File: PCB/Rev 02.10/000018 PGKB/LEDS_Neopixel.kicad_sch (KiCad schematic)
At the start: 15 parts

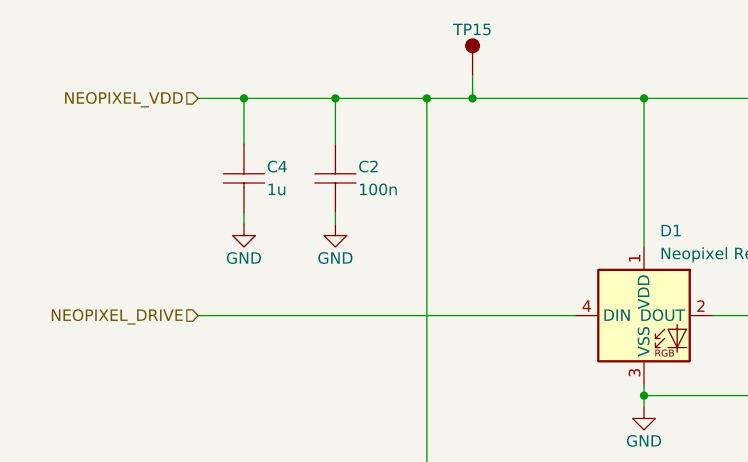
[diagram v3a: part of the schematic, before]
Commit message: Resolved DRC problems
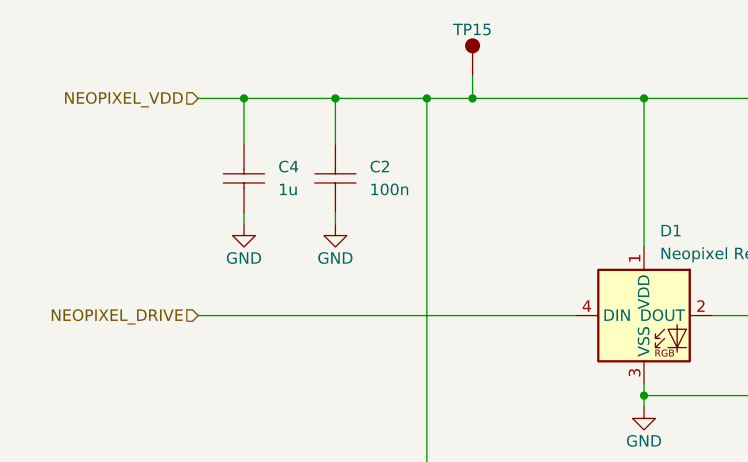
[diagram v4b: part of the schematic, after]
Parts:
- C4: Code 1u -> (none)
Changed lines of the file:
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@@
 			)
 		)
-		(property "Description" ""
+		(property "Description" "Power symbol creates a global label with name \"GND\" , ground"
 			(at 127 172.72 0)
 			(effects
@@
 		(on_board yes)
 		(dnp no)
+		(fields_autoplaced yes)
 		(property "Reference" "C2"
-			(at 95.25 31.75 0)
+			(at 96.52 31.7499 0)
 			(effects
 				(font
@@
 		)
 		(property "Value" "100n"
-			(at 95.25 34.29 0)
+			(at 96.52 34.2899 0)
 			(effects
 				(font
@@
 			)
 		)
-		(property "Description" ""
+		(property "Description" "CAP CER 0.1UF 50V X7R 0603"
 			(at 92.71 33.02 0)
 			(effects
@@
 			)
 		)
-		(property "Description" ""
+		(property "Description" "Power symbol creates a global label with name \"GND\" , ground"
 			(at 127 134.62 0)
 			(effects
@@
 		(on_board yes)
 		(dnp no)
+		(fields_autoplaced yes)
 		(property "Reference" "C4"
-			(at 85.09 31.75 0)
+			(at 86.36 31.7499 0)
 			(effects
 				(font
@@
 		)
 		(property "Value" "1u"
-			(at 69.85 1.27 0)
-			(effects
-				(font
-					(size 1.27 1.27)
-				)
-				(justify left)
-				(hide yes)
+			(at 86.36 34.2899 0)
+			(effects
+				(font
+					(size 1.27 1.27)
+				)
+				(justify left)
 			)
 		)
@@
 			)
 		)
-		(property "Description" ""
-			(at 82.55 33.02 0)
-			(effects
-				(font
-					(size 1.27 1.27)
-				)
-				(hide yes)
-			)
-		)
-		(property "Code" "1u"
-			(at 85.09 34.29 0)
-			(effects
-				(font
-					(size 1.27 1.27)
-				)
-				(justify left)
+		(property "Description" "CAP CER 1UF 25V X7R 0805"
+			(at 69.85 1.27 0)
+			(effects
+				(font
+					(size 1.27 1.27)
+				)
+				(justify left)
+				(hide yes)
 			)
 		)
@@
 			)
 		)
-		(property "Description" ""
+		(property "Description" "Test point"
 			(at 107.95 21.59 0)
 			(effects
@@
 			)
 		)
-		(property "Description" ""
+		(property "Description" "Power symbol creates a global label with name \"GND\" , ground"
 			(at 127 58.42 0)
 			(effects
@@
 			)
 		)
-		(property "Description" ""
+		(property "Description" "Power symbol creates a global label with name \"GND\" , ground"
 			(at 92.71 38.1 0)
 			(effects
@@
 			)
 		)
-		(property "Description" ""
+		(property "Description" "Power symbol creates a global label with name \"GND\" , ground"
 			(at 82.55 38.1 0)
 			(effects
@@
 			)
 		)
-		(property "Description" ""
+		(property "Description" "Power symbol creates a global label with name \"GND\" , ground"
 			(at 127 96.52 0)
 			(effects
@@
 			)
 		)
-		(property "Description" ""
+		(property "Description" "Test point"
 			(at 116.84 139.7 0)
 			(effects
